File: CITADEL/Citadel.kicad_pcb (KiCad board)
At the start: 2 copper layers, 130 x 105 mm, 55 parts, among them J11 Camera 1, J12 Camera 2, J14 5V Swtich Power, J18 CAN BUS, J19 Battery Connections, J20 Servo 1, J21 Servo 2, J22 Servo 3, J23 Stepper Motors 3, J24 Stepper Motors 4, J25 LSS Servo, J26 Vibration Motor, J27 Stepper Motors 1, J28 Stepper Motors 2, M10 Fan 1, M11 Fan 2, M12 Fan 3, Q4 SSM3K329R_LF, Q5 SSM3K329R_LF, Q6 SSM3K329R_LF, Q7 SSM3K329R_LF, U1 MAX7315AUE_T, U3 TJA1051T-3, U4 RASPBERRY_PI_4B_4GB

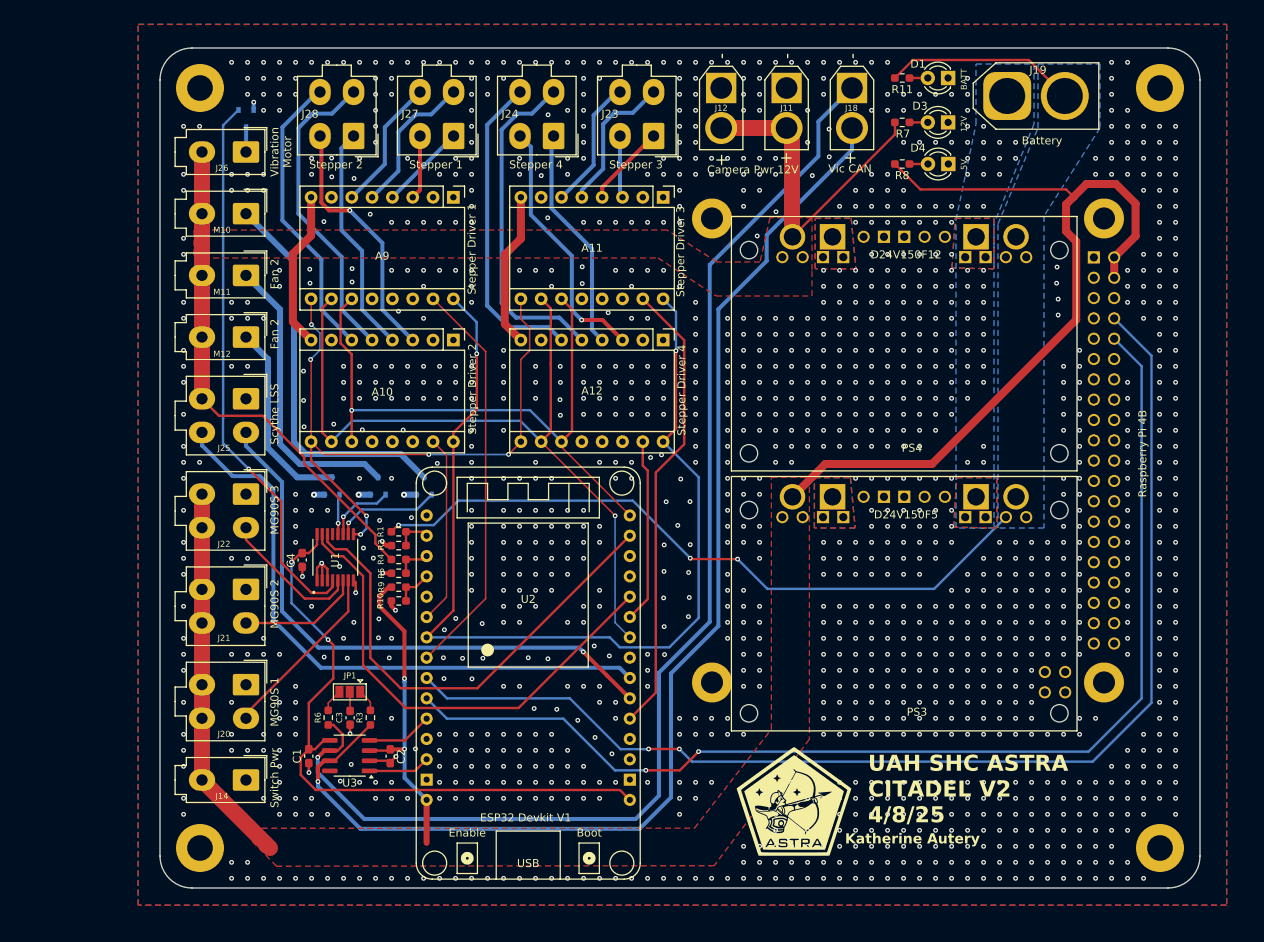
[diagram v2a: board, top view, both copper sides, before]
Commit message: CITADEL 2025 V3
May 11, 2025; got rid of the GPIO extender
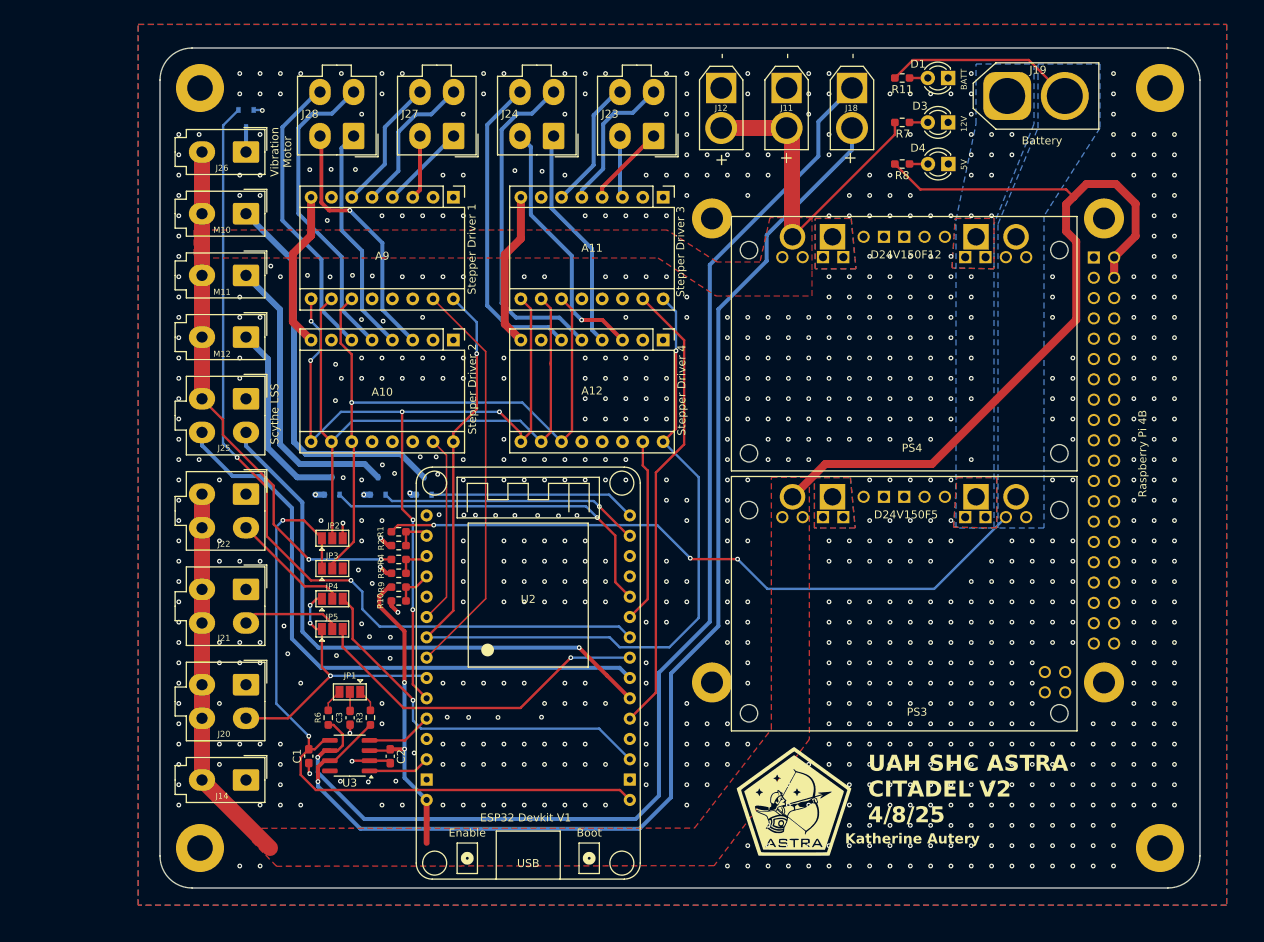
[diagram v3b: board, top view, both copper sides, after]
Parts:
- removed C4: 0.047uF, Capacitor_SMD:C_0603_1608Metric_Pad1.08x0.95mm_HandSolder
- removed U1: MAX7315AUE_T, Citadel:MAX7315AUE+T
- added JP2: SolderJumper_3_Open, Jumper:SolderJumper-3_P1.3mm_Open_Pad1.0x1.5mm, F.Cu at (99.5, 101.3)
- added JP3: SolderJumper_3_Open, Jumper:SolderJumper-3_P1.3mm_Open_Pad1.0x1.5mm, F.Cu at (99.5, 105.1)
- added JP4: SolderJumper_3_Open, Jumper:SolderJumper-3_P1.3mm_Open_Pad1.0x1.5mm, F.Cu at (99.5, 108.8)
- added JP5: SolderJumper_3_Open, Jumper:SolderJumper-3_P1.3mm_Open_Pad1.0x1.5mm, F.Cu at (99.5, 112.6)
- R2: value 3.1 kΩ -> 2.21 kΩ
- R5: value 3.8 kΩ -> 3.32 kΩ
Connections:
- U2 pad 10: /RASPI_TX -> /Step_Motor_Enable
- U2 pad 18: unconnected-(U2-GPIO15/A13-Pad18) -> /MG90S3_T
- U2 pad 23: unconnected-(U2-GPIO05/CS-Pad23) -> /MG90S2_T
- U2 pad 24: /M0 -> /VibMotorSignal
- U2 pad 26: /MAX_SDA -> /Fan3MosSignal
- U2 pad 29: /MAX_SCL -> /Fan2MosSignal
- U2 pad 30: /M1 -> /Fan1MosSignal
- U2 pad 9: /RASPI_RX -> /MG90S1
- U4 pad 10: /RASPI_TX -> unconnected-(U4-GPIO15/RXD0-Pad10)
- U4 pad 8: /RASPI_RX -> unconnected-(U4-GPIO14/TXD0-Pad8)
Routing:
- net /RASPI_RX: track 148.0 -> 0.00 mm, vias 2 -> 0
- net /RASPI_TX: track 143.2 -> 0.00 mm, vias 2 -> 0
- net /MAX_SDA: track 60.4 -> 0.00 mm
- net /MAX_SCL: track 60.4 -> 0.00 mm
- net /MG90S3_T: track 0.00 -> 48.0 mm, vias 0 -> 1
- net /MG90S2_T: track 0.00 -> 43.9 mm, vias 0 -> 1
- net /Fan3MosSignal: track 5.03 -> 45.2 mm
- net /VibMotorSignal: track 69.5 -> 108.2 mm, vias 1 -> 2
- net /Step_Motor_Enable: track 81.1 -> 105.2 mm
- net /Fan2MosSignal: track 8.61 -> 32.7 mm
- net /M0: track 95.3 -> 78.5 mm, vias 1 -> 0
- net /MG90S1: track 22.5 -> 37.0 mm, vias 0 -> 3
- net /Fan1MosSignal: track 13.4 -> 26.0 mm, vias 1 -> 0
- net +3.3V: track 81.4 -> 89.4 mm
- net GND: track 25.3 -> 18.5 mm, vias 1416 -> 881
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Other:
- board text removed: "Camera Pwr 12V"
- board text removed: "Fan 2"
- board text removed: "MG90S 1"
- board text removed: "MG90S 2"
- board text removed: "MG90S 3"
- board text removed: "Stepper 1"
- board text removed: "Stepper 2"
- board text removed: "Stepper 3"
- board text removed: "Stepper 4"
- board text removed: "Switch Pwr"
- board text removed: "Vic CAN"
